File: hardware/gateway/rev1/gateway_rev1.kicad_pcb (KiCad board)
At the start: 2 copper layers, 100 x 45 mm, 79 parts, among them IC1 STM8L151K4T6, IC2 CC1101RGPR, IC3 LT1615ES5-1#TRMPBF, IC4 MIC4427YM, IC5 MB85RC64TAPNF-G-BDERE1, J1 G8250041000YEU, J2 M20-9770342, Q1 IRLML6402TRPBF, U1 2462, Y1 NX3225GA-26.000M-STD-CRG-2

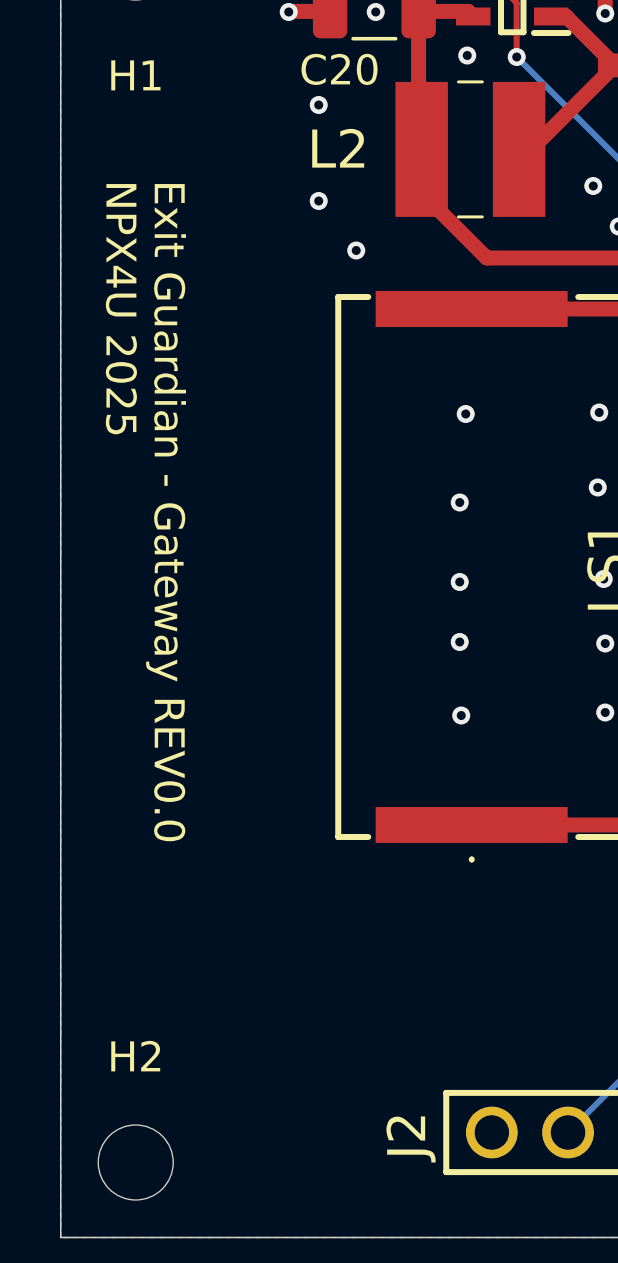
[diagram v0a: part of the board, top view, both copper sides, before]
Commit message: Changed all references from REV0 to REV1 and update PCB silk screen.
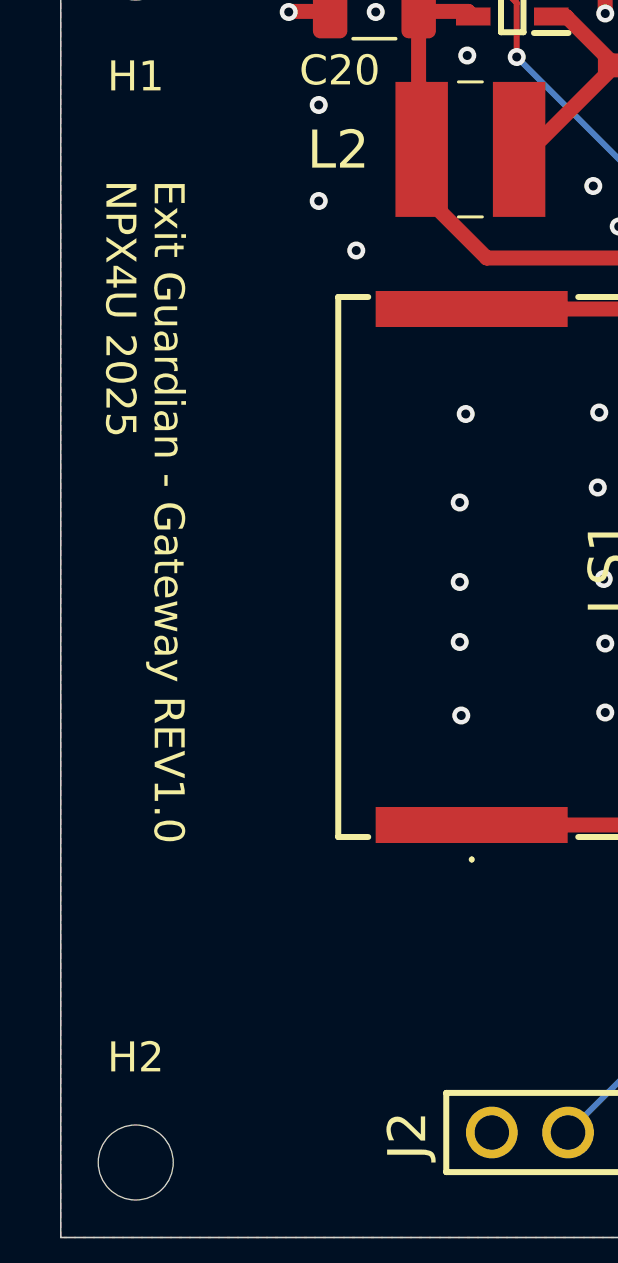
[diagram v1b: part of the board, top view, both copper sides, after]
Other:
- board text added: "Exit Guardian - Gateway REV1.0 NPX4U 2025"
- board text removed: "Exit Guardian - Gateway REV0.0 NPX4U 2025"
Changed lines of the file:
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@@
 	(title_block
 		(title "Gateway")
-		(date "2025-10-07")
-		(rev "REV0.0")
+		(date "2025-10-20")
+		(rev "REV1.0")
 		(company "NPX4U")
 	)
@@
 		(layer "Edge.Cuts")
 	)
-	(gr_text "Exit Guardian - Gateway REV0.0\nNPX4U 2025"
+	(gr_text "Exit Guardian - Gateway REV1.0\nNPX4U 2025"
 		(at 180.9 124.7 270)
 		(layer "F.SilkS")

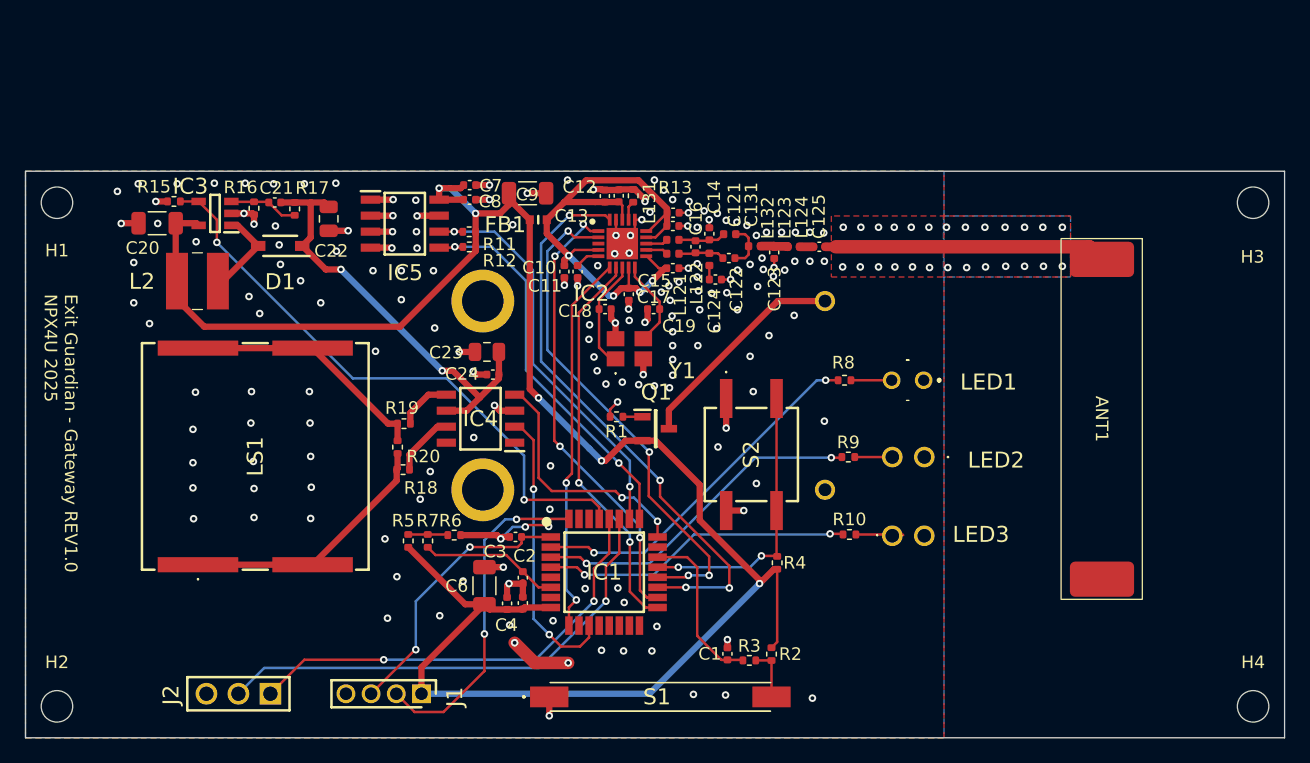
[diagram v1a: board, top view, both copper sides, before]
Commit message: RF passive components placed in the right relative positions.
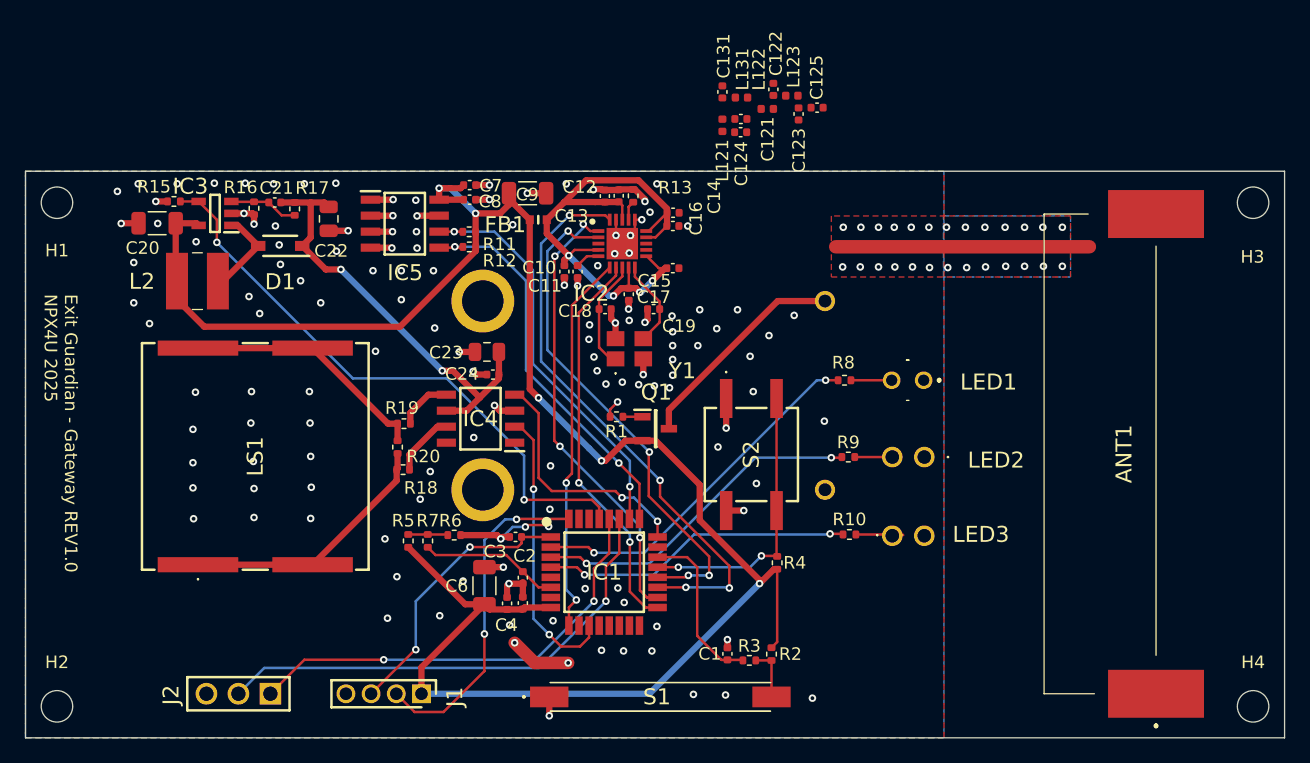
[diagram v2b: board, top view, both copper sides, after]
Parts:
- removed L124: 12nH, Inductor_SMD:L_0402_1005Metric
- removed L132: 18nH, Inductor_SMD:L_0402_1005Metric
- ANT1: value ANT-868-HESM -> ANT-433-HESM; footprint MyParts:ANT-868-HESM -> MyParts:ANT433HESM
- C121: value 1pF -> 3.9pF
- C122: value 1.5pF -> 8.2pF
- C123: value 3.3pF -> 5.6pF
- C124: value 100pF -> 220pF
- C125: value 12pF -> 220pF
- C131: value 1.5pF -> 3.9pF
- L121, L123, L131: value 12nH -> 27nH
- L122: value 18nH -> 22nH
- moved C122 13.9 mm to (238.9, 108.5), turned to -90 degrees
- moved L122 12.8 mm to (238.4, 110.0), turned to 0 degrees
- moved L131 12.5 mm to (236.4, 109.1)
- moved L123 12.3 mm to (240.4, 109.0)
- moved C124 11.9 mm to (236.3, 111.8)
- moved C131 11.3 mm to (234.8, 108.7)
- moved C123 11.2 mm to (240.9, 110.4)
- moved C125 11.1 mm to (242.4, 109.9)
- moved L121 10.9 mm to (234.8, 111.3), turned to -90 degrees
- moved C121 10.8 mm to (236.3, 110.8), turned to 180 degrees
- moved ANT1 5.36 mm to (260.4, 137.4), turned to 90 degrees
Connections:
- C121 pad 2: Net-(C121-Pad2) -> Net-(IC2-RF_P)
- C122 pad 1: Net-(C121-Pad1) -> GND
- C125 pad 1: Net-(C125-Pad1) -> Net-(C123-Pad2)
- C131 pad 1: Net-(C121-Pad2) -> Net-(IC2-RF_N)
- L121 pad 2: Net-(C121-Pad1) -> Net-(C124-Pad2)
- L122 pad 2: Net-(C124-Pad2) -> Net-(C122-Pad2)
- L131 pad 2: Net-(C121-Pad2) -> Net-(C121-Pad1)
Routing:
- net GND: track 73.4 -> 69.1 mm, vias 205 -> 166
- net Net-(C121-Pad2): track 3.79 -> 0.00 mm
- net Net-(C121-Pad1): track 3.69 -> 0.00 mm
- net Net-(C122-Pad2): track 3.67 -> 0.00 mm
- net /RF/RF_LINE: track 22.4 -> 20.2 mm
- net Net-(C123-Pad2): track 2.15 -> 0.00 mm
- net Net-(IC2-RF_P): track 1.75 -> 0.00 mm
- net Net-(IC2-RF_N): track 1.75 -> 0.00 mm
- net Net-(C124-Pad2): track 1.11 -> 0.00 mm
- net Net-(C125-Pad1): track 1.06 -> 0.00 mm

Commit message: All connections performed. Still with DRC errors on antenna footprint.
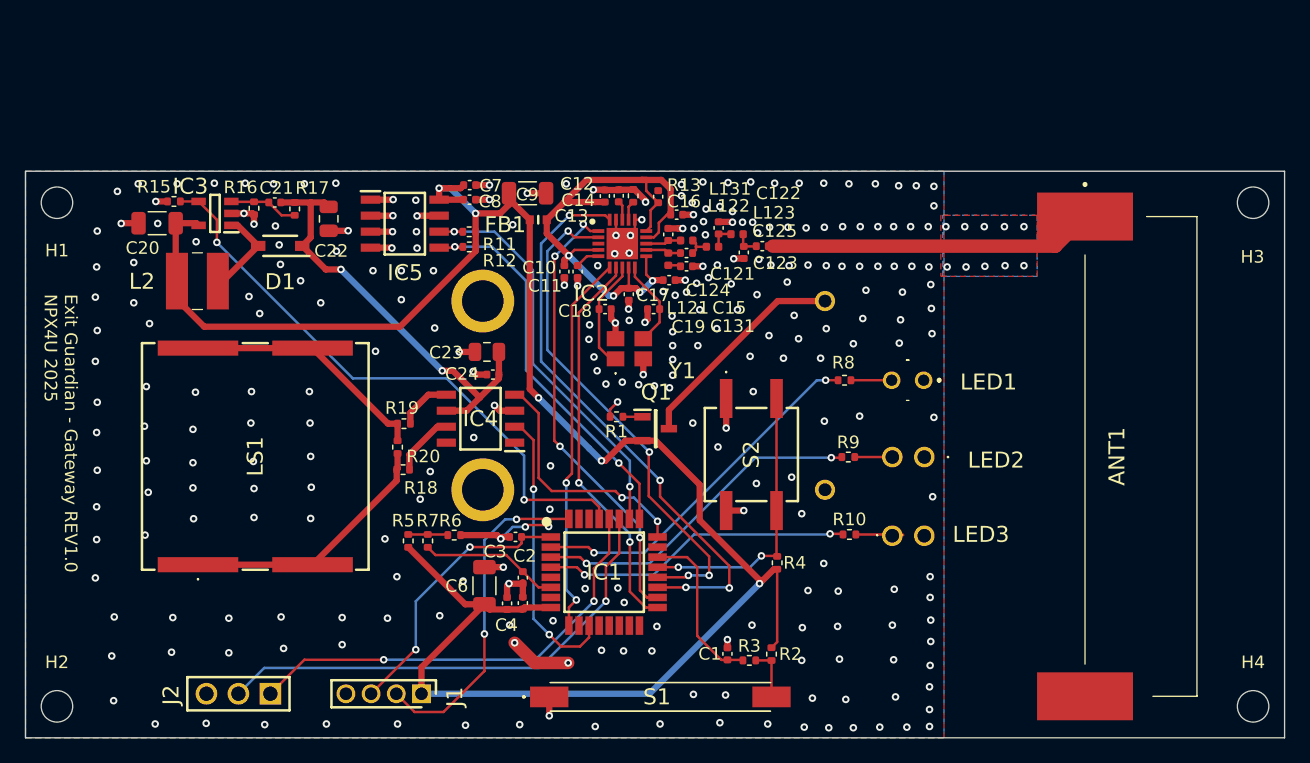
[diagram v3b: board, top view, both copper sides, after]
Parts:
- moved L131 12.2 mm to (232.0, 120.5)
- moved ANT1 12.1 mm to (272.5, 137.6), turned to -90 degrees
- moved C131 12.1 mm to (230.6, 120.0)
- moved L123 11.8 mm to (236.0, 120.0)
- moved C122 11.8 mm to (234.6, 119.5)
- moved C123 11.8 mm to (236.6, 121.4)
- moved C125 11.8 mm to (238.0, 120.9)
- moved L122 11.8 mm to (234.1, 121.0)
- moved C121 11.5 mm to (232.0, 121.5)
- moved C124 11.5 mm to (232.0, 122.5)
- moved L121 11.5 mm to (230.6, 121.9)
- moved C14 1.74 mm to (229.8, 117.0), turned to 90 degrees
- moved C15 0.99 mm to (230.6, 123.6)
- moved C16 0.95 mm to (231.2, 118.4)
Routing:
- net GND: track 69.1 -> 74.9 mm, vias 166 -> 290
- net /RF/RF_LINE: track 20.2 -> 25.8 mm
- net RF_VDD: track 44.3 -> 47.3 mm
- net Net-(IC2-RF_P): track 0.00 -> 2.84 mm
- net Net-(IC2-RF_N): track 0.00 -> 2.83 mm
- net Net-(C121-Pad1): track 0.00 -> 2.18 mm
- net Net-(C122-Pad2): track 0.00 -> 2.06 mm
- net Net-(C123-Pad2): track 0.00 -> 1.99 mm
- net Net-(C124-Pad2): track 0.00 -> 1.00 mm

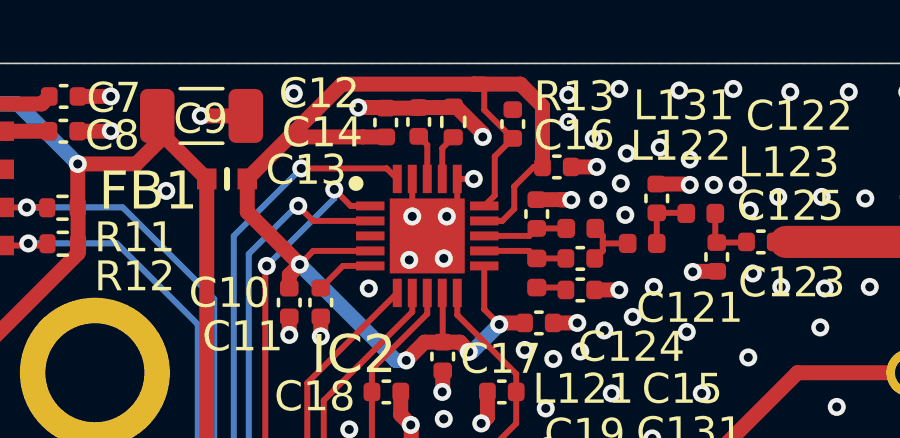
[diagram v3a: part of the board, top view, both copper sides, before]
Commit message: All connections finished, no DRC erros, gerbers and, components position and BOM generated.
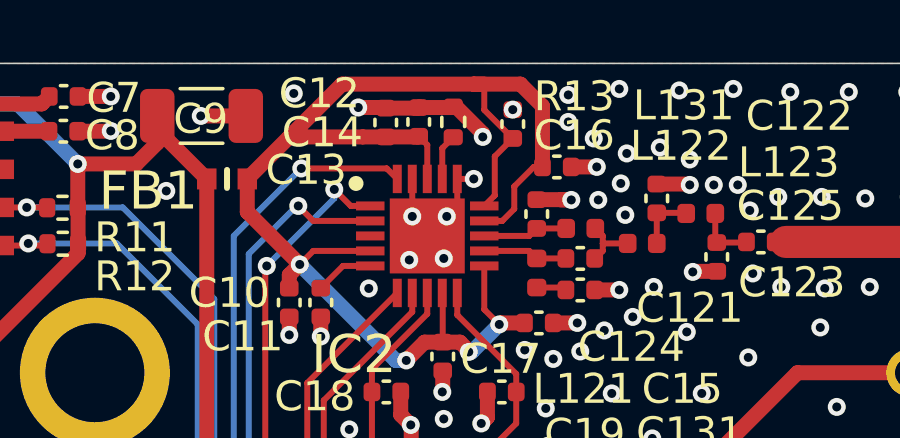
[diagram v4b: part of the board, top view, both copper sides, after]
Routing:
- net RF_VDD: track 47.3 -> 48.4 mm
- net GND: vias 290 -> 291
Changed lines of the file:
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@@
 			(layer "F.SilkS")
 		)
-		(fp_line
-			(start -21.955 13.7)
-			(end -21.955 -1)
-			(stroke
-				(width 0.1)
-				(type solid)
-			)
-			(layer "F.CrtYd")
-		)
-		(fp_line
-			(start -21.955 13.7)
-			(end -21.955 -1)
-			(stroke
-				(width 0.1)
-				(type solid)
-			)
-			(layer "F.CrtYd")
-		)
-		(fp_line
-			(start 21.955 13.7)
-			(end -21.955 13.7)
+		(fp_rect
+			(start -21.95 -1)
+			(end 21.95 13.65)
 			(stroke
-				(width 0.1)
-				(type solid)
-			)
-			(layer "F.CrtYd")
-		)
-		(fp_line
-			(start 21.955 13.7)
-			(end -21.955 13.7)
-			(stroke
-				(width 0.1)
-				(type solid)
-			)
-			(layer "F.CrtYd")
-		)
-		(fp_line
-			(start -21.955 -1)
-			(end 21.955 -1)
-			(stroke
-				(width 0.1)
-				(type solid)
-			)
-			(layer "F.CrtYd")
-		)
-		(fp_line
-			(start -21.955 -1)
-			(end 21.955 -1)
-			(stroke
-				(width 0.1)
-				(type solid)
-			)
-			(layer "F.CrtYd")
-		)
-		(fp_line
-			(start 21.955 -1)
-			(end 21.955 13.7)
-			(stroke
-				(width 0.1)
-				(type solid)
-			)
-			(layer "F.CrtYd")
-		)
-		(fp_line
-			(start 21.955 -1)
-			(end 21.955 13.7)
-			(stroke
-				(width 0.1)
-				(type solid)
+				(width 0.05)
+				(type default)
 			)
+			(fill no)
 			(layer "F.CrtYd")
 		)
@@
 	)
 	(via
+		(at 229.75 116.49)
+		(size 0.6)
+		(drill 0.3)
+		(layers "F.Cu" "B.Cu")
+		(net 1)
+	)
+	(via
 		(at 210.55 119.75)
 		(size 0.6)
@@
 	)
 	(segment
+		(start 226.595 117.4)
+		(end 226.615 117.38)
+		(width 0.5)
+		(layer "F.Cu")
+		(net 7)
+	)
+	(segment
 		(start 228.8 119.7)
 		(end 229.005 119.7)
@@
 	)
 	(segment
+		(start 225.515 117.4)
+		(end 226.595 117.4)
+		(width 0.5)
+		(layer "F.Cu")
+		(net 7)
+	)
+	(segment
 		(start 224.75 117.4)
 		(end 222.3 117.4)
@@
 		(layer "F.Cu")
 		(net 7)
-	)
-	(segment
-		(start 226.595 117.4)
-		(end 226.615 117.38)
-		(width 0.5)
-		(layer "F.Cu")
-		(net 7)

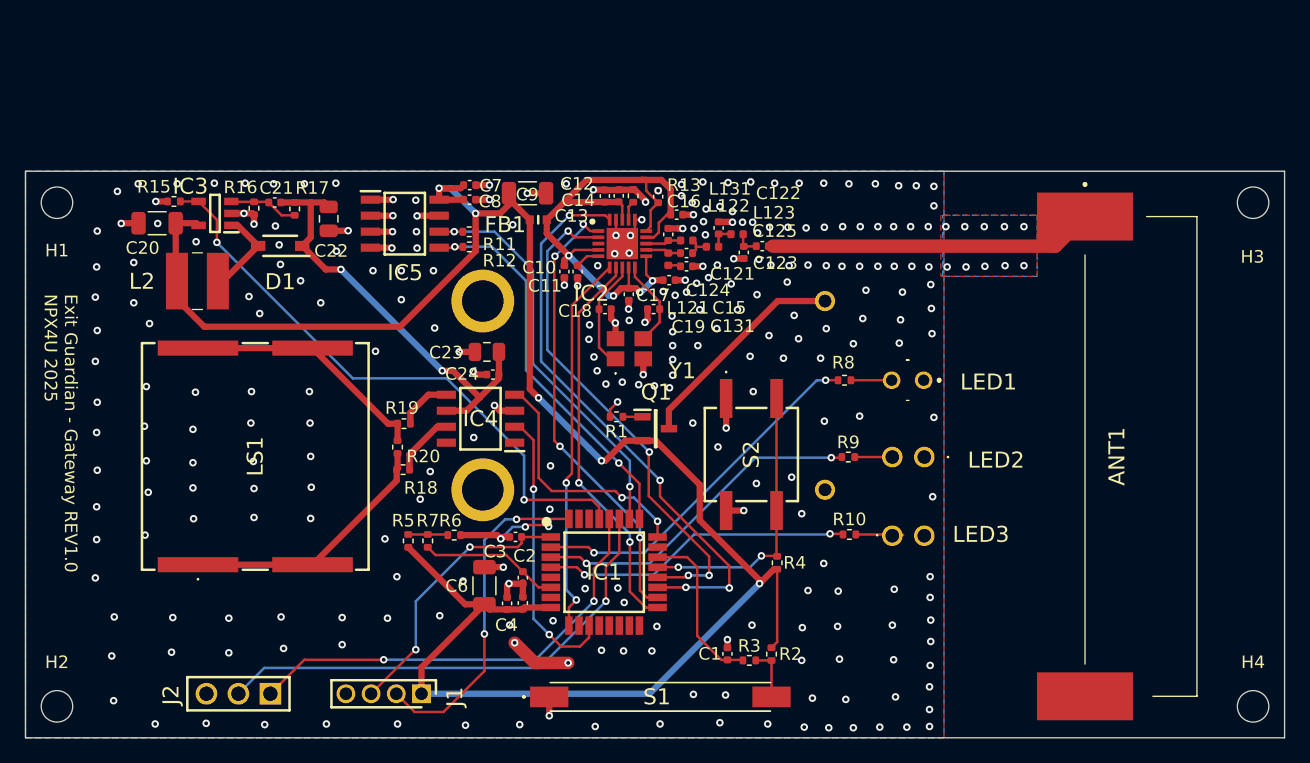
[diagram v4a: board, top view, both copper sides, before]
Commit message: Added the 3 fiducial points for pick and place machine.
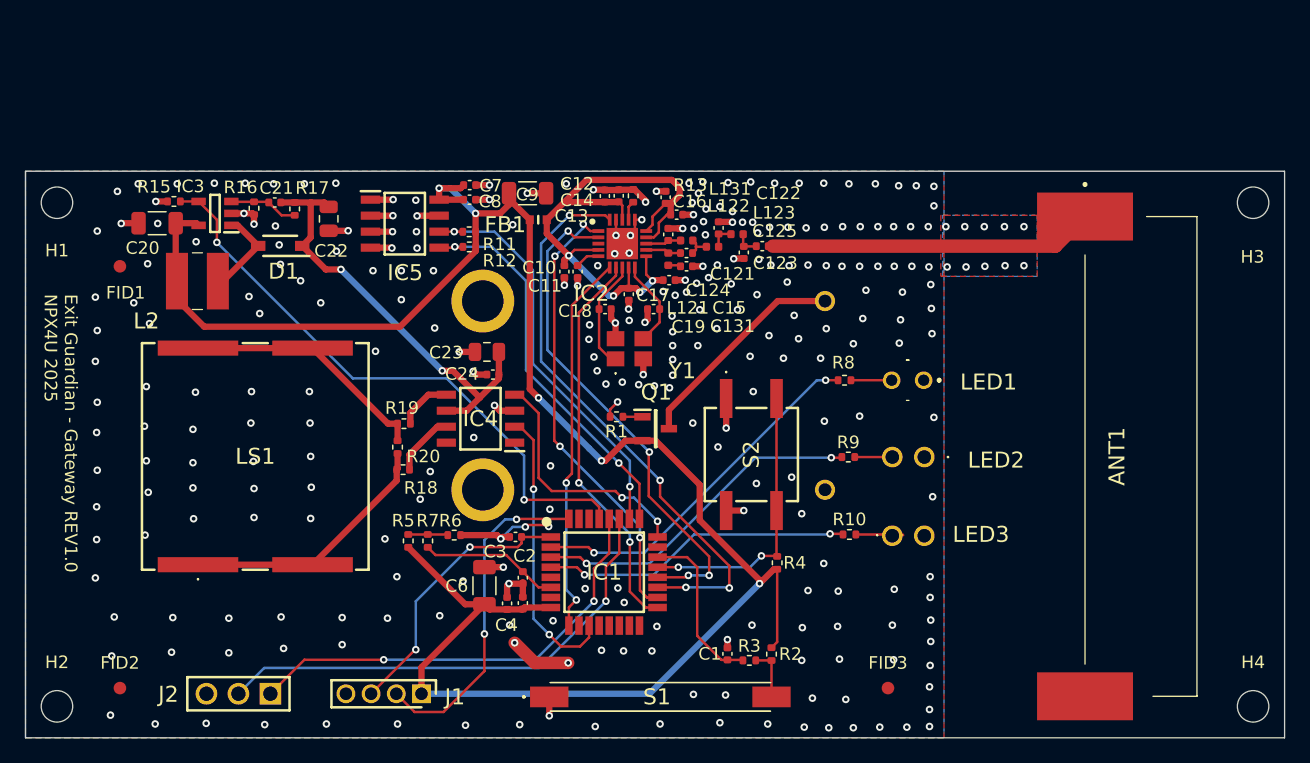
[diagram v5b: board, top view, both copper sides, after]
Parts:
- added FID1: Fiducial, Fiducial:Fiducial_1mm_Mask2mm, F.Cu at (187.0, 122.5)
- added FID2: Fiducial, Fiducial:Fiducial_1mm_Mask2mm, F.Cu at (187.0, 156.0)
- added FID3: Fiducial, Fiducial:Fiducial_1mm_Mask2mm, F.Cu at (248.0, 156.0)
- moved C14 0.60 mm to (230.3, 117.0)
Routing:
- net RF_VDD: track 48.4 -> 47.6 mm
- net GND: track 74.9 -> 75.7 mm, vias 291 -> 289
